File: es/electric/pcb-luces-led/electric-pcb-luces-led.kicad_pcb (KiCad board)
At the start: 2 copper layers, 59.7 x 39.4 mm, 28 parts, among them SW1 SW_SPDT, U1 74HC14

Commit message: Cambios a 17/03/2022
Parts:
- M3 (x4): value (none) -> Val**
- moved BT1 0.63 mm to (53.3, 61.6)
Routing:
- net +BATT: track 123.5 -> 133.5 mm

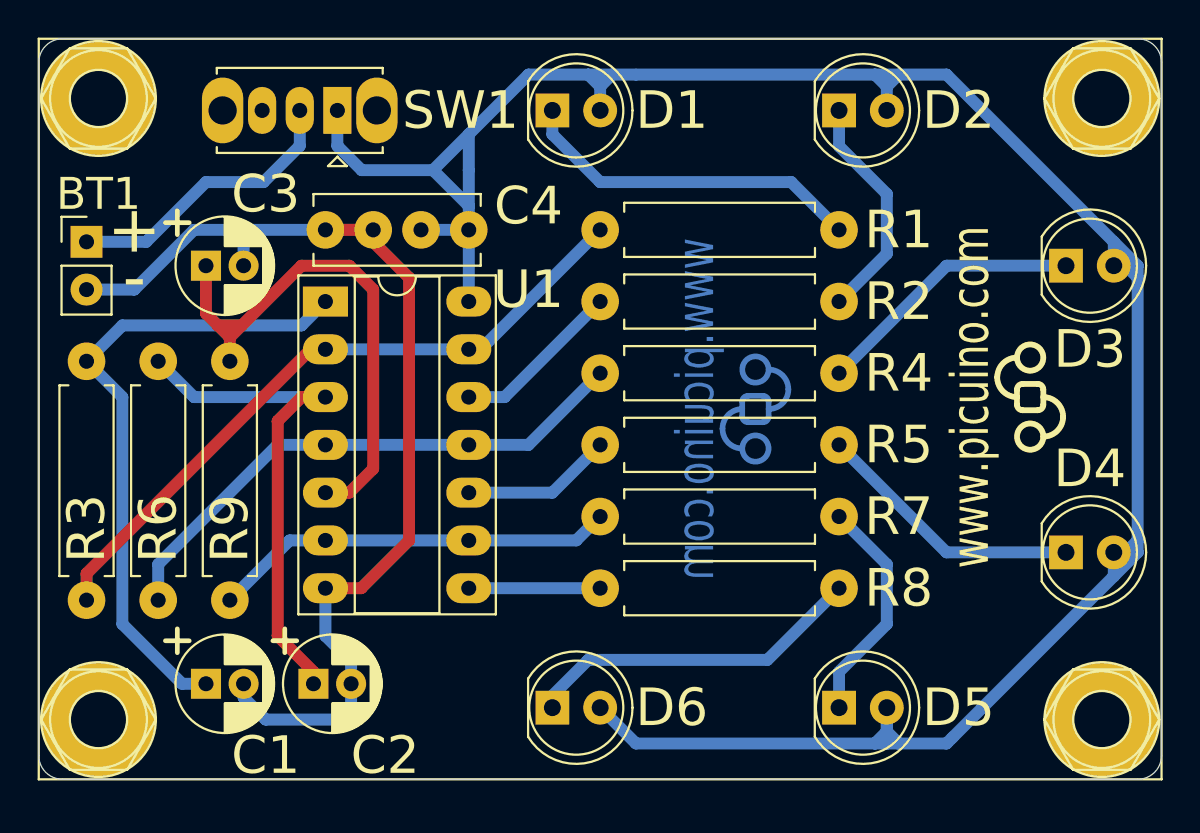
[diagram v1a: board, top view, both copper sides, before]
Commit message: Trasladar proyectos KiCAD 5 a KiCAD 6. Thickness 12mils
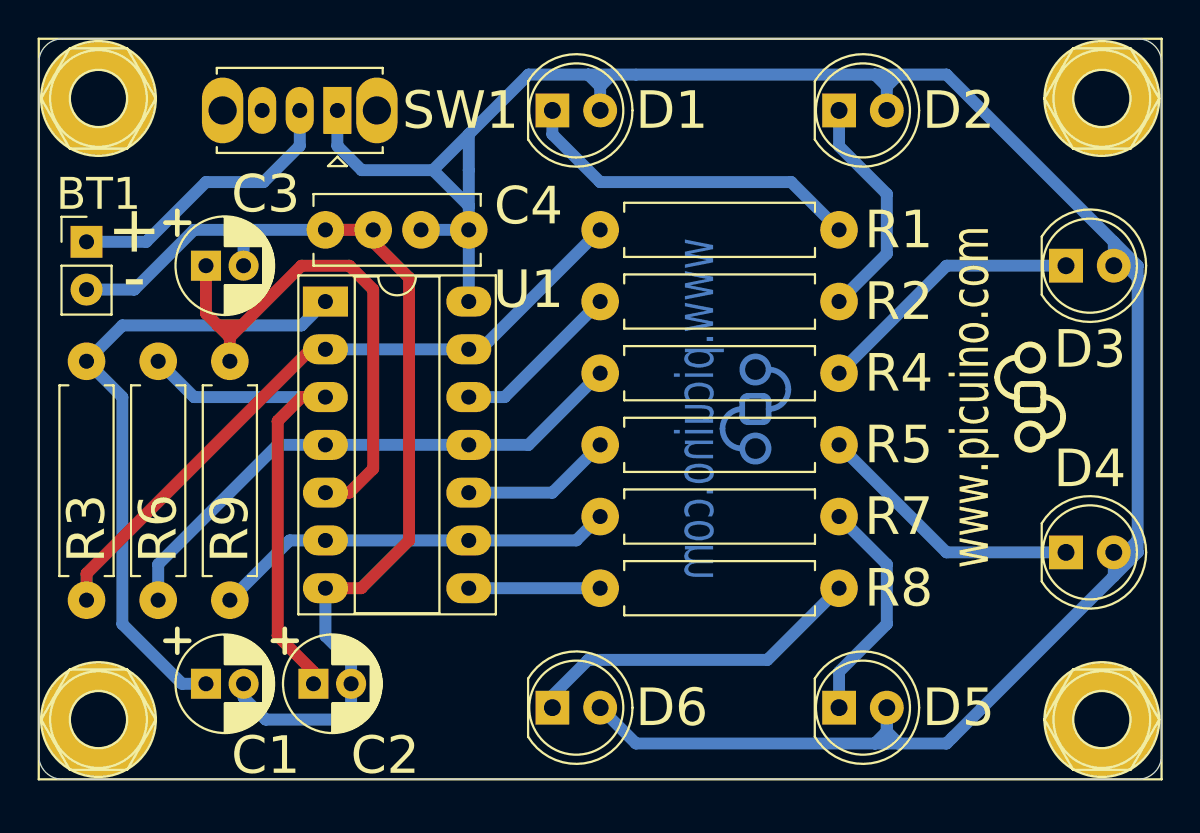
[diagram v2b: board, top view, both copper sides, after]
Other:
- net class Default removed
